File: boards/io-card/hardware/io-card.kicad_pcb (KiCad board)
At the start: 2 copper layers, 100 x 100 mm, 139 parts, among them J10 STACK BUS, J11 RACK 12V, J30 RELAY, J40 IO, J50 ANALOG OUT, K1 AQW212, K2 AQW212, U90 ISO1540, U91 MC78L05, U92 MCP4728, U93 OPA4171

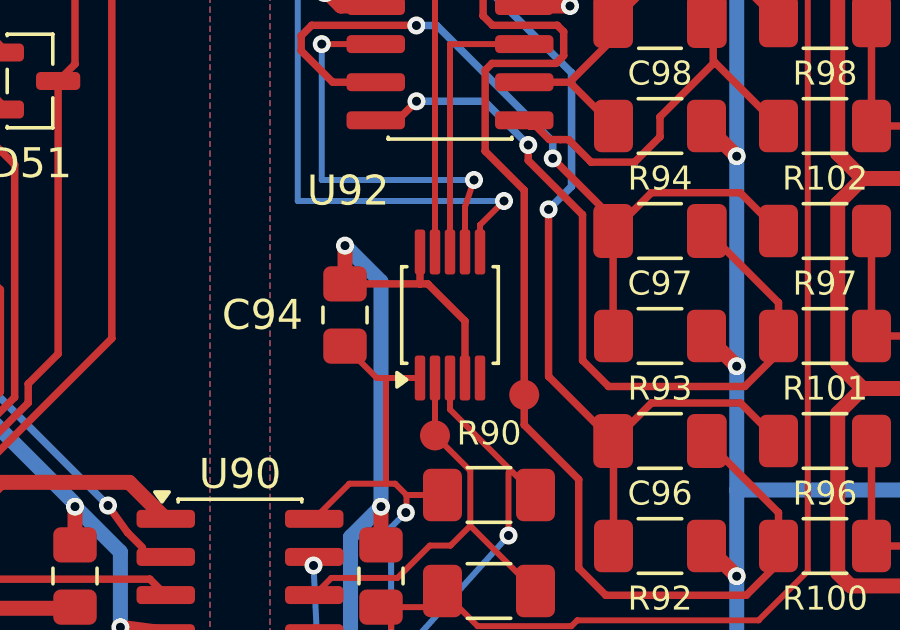
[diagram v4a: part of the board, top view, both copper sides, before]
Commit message: io-card: U92 MSOP-10 pads narrowed to 0.30 mm for PCBWay's mask web
PCBWay (order W517176ASE106) needs >= 0.19 mm between IC pads for a green
solder-mask web; the stock MSOP-10 pads (0.35 mm) left 0.15 mm. New
Thl_Package:MSOP-10_3x3mm_P0.5mm_Pad0.30 (stock footprint, 0.30 mm pads
per Microchip's MSOP-10 UN land pattern, 0.20 mm gap), built by
lib/footprint_src/Thl_Package/msop10_pad030.py. U92 tracks (0.20/0.25 mm)
still land inside the pads; check_board clean. No other pad gap under
0.19 mm on the six ordered boards.

Co-Authored-By: Claude Opus 5.5 <noreply@anthropic.com>
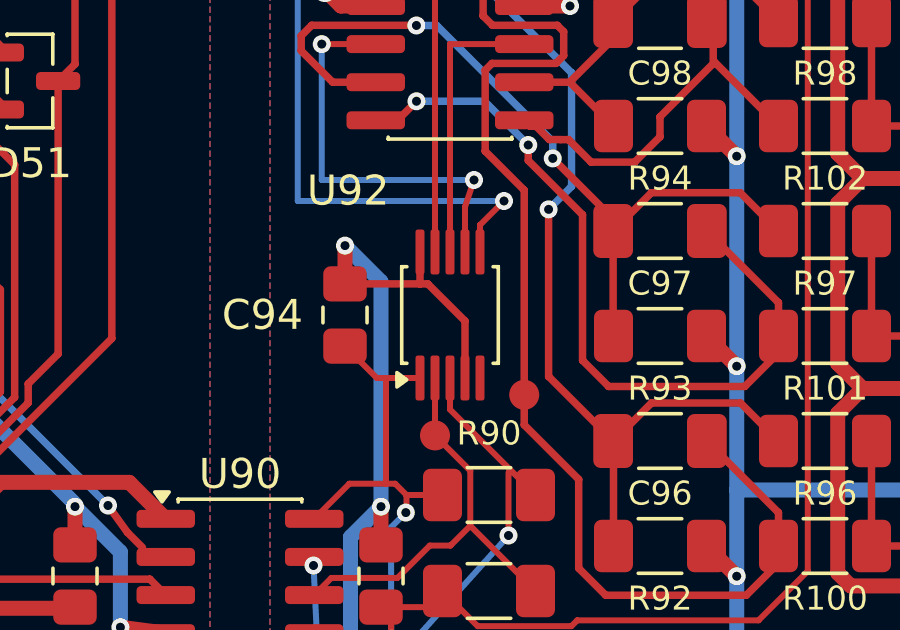
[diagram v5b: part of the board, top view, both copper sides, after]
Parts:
- U92: footprint Package_SO:MSOP-10_3x3mm_P0.5mm -> Thl_Package:MSOP-10_3x3mm_P0.5mm_Pad0.30
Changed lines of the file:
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@@
 		(embedded_fonts no)
 	)
-	(footprint "Package_SO:MSOP-10_3x3mm_P0.5mm"
+	(footprint "Thl_Package:MSOP-10_3x3mm_P0.5mm_Pad0.30"
 		(layer "F.Cu")
 		(at 168.5 128.8 90)
@@
 		(pad "1" smd roundrect
 			(at -2.1 -1 90)
-			(size 1.5 0.35)
+			(size 1.5 0.3)
 			(layers "F.Cu" "F.Mask" "F.Paste")
 			(roundrect_rratio 0.25)
@@
 		(pad "2" smd roundrect
 			(at -2.1 -0.5 90)
-			(size 1.5 0.35)
+			(size 1.5 0.3)
 			(layers "F.Cu" "F.Mask" "F.Paste")
 			(roundrect_rratio 0.25)
@@
 		(pad "3" smd roundrect
 			(at -2.1 0 90)
-			(size 1.5 0.35)
+			(size 1.5 0.3)
 			(layers "F.Cu" "F.Mask" "F.Paste")
 			(roundrect_rratio 0.25)
@@
 		(pad "4" smd roundrect
 			(at -2.1 0.5 90)
-			(size 1.5 0.35)
+			(size 1.5 0.3)
 			(layers "F.Cu" "F.Mask" "F.Paste")
 			(roundrect_rratio 0.25)
@@
 		(pad "5" smd roundrect
 			(at -2.1 1 90)
-			(size 1.5 0.35)
+			(size 1.5 0.3)
 			(layers "F.Cu" "F.Mask" "F.Paste")
 			(roundrect_rratio 0.25)
@@
 		(pad "6" smd roundrect
 			(at 2.1 1 90)
-			(size 1.5 0.35)
+			(size 1.5 0.3)
 			(layers "F.Cu" "F.Mask" "F.Paste")
 			(roundrect_rratio 0.25)
@@
 		(pad "7" smd roundrect
 			(at 2.1 0.5 90)
-			(size 1.5 0.35)
+			(size 1.5 0.3)
 			(layers "F.Cu" "F.Mask" "F.Paste")
 			(roundrect_rratio 0.25)
@@
 		(pad "8" smd roundrect
 			(at 2.1 0 90)
-			(size 1.5 0.35)
+			(size 1.5 0.3)
 			(layers "F.Cu" "F.Mask" "F.Paste")
 			(roundrect_rratio 0.25)
@@
 		(pad "9" smd roundrect
 			(at 2.1 -0.5 90)
-			(size 1.5 0.35)
+			(size 1.5 0.3)
 			(layers "F.Cu" "F.Mask" "F.Paste")
 			(roundrect_rratio 0.25)
@@
 		(pad "10" smd roundrect
 			(at 2.1 -1 90)
-			(size 1.5 0.35)
-			(layers "F.Cu" "F.Mask" "F.Paste")
-			(roundrect_rratio 0.25)
+			(size 1.5 0.3)
+			(layers "F.Cu" "F.Mask" "F.Paste")
+			(roundrect_rratio 0.25)
